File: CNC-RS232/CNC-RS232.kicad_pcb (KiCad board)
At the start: 2 copper layers, 100 x 80 mm, 50 parts, among them J1 DIN-5_180degree, J2 DIN-5_180degree, J3 DIN-5_180degree, J4 DIN-5_180degree, J5 DIN-5_180degree, Q1 BC547, Q2 BC557, Q3 BC547, Q4 BC547, U1 L7805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

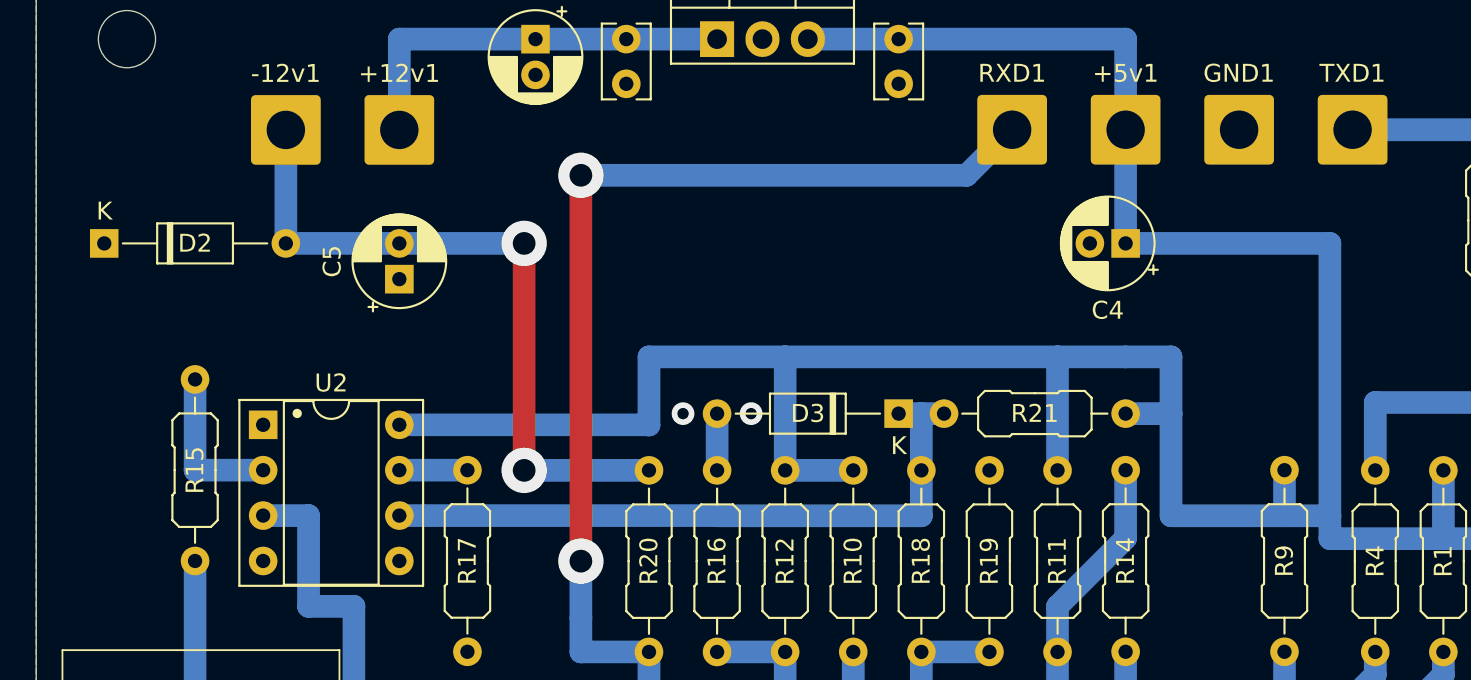
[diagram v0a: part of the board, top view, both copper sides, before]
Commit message: fixed RS232 and Thru
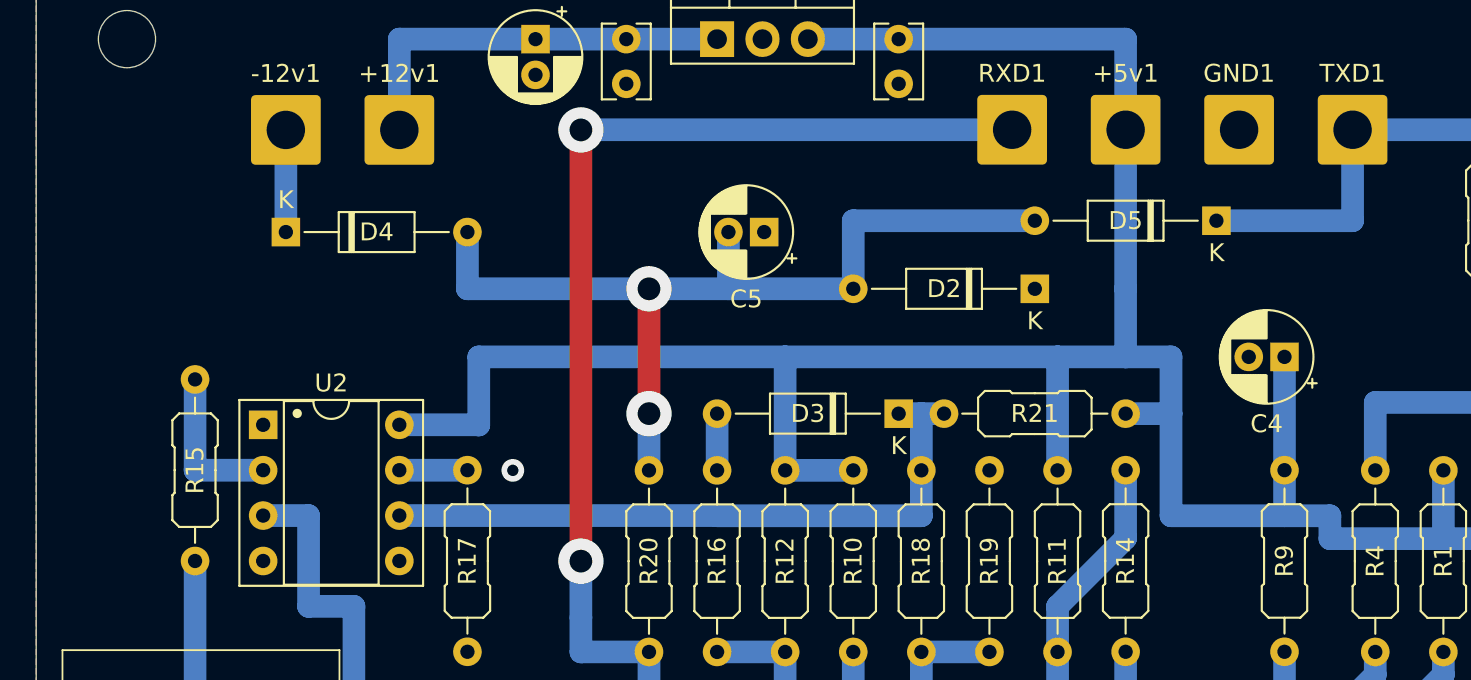
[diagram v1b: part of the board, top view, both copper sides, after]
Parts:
- added D4: 1N4148, Diode_THT:D_DO-35_SOD27_P10.16mm_Horizontal, F.Cu at (26.7, 28.6)
- added D5: 1N4148, Diode_THT:D_DO-35_SOD27_P10.16mm_Horizontal, F.Cu at (78.7, 27.9)
- moved D2 52.1 mm to (68.6, 31.8), turned to 180 degrees
- moved C5 20.6 mm to (53.4, 28.6), turned to 180 degrees
- moved C4 10.9 mm to (82.5, 35.6)
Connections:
- C5 pad 2: Net-(-12v1-Pin_1) -> Net-(D2-A)
- D2 pad 2: Net-(-12v1-Pin_1) -> Net-(D2-A)
- R20 pad 1: Net-(-12v1-Pin_1) -> Net-(D2-A)
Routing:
- net Net-(D2-A): track 0.00 -> 52.1 mm, vias 0 -> 2
- net Net-(-12v1-Pin_1): track 39.4 -> 5.71 mm, vias 2 -> 0
- net +5V: track 176.6 -> 162.6 mm
- net Net-(D5-K): track 7.62 -> 20.3 mm
- net Net-(Q2-C): track 63.6 -> 65.0 mm
- net GND: vias 2 -> 1

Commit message: PCB cleanup
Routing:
- net Net-(Q2-C): track 65.0 -> 64.3 mm
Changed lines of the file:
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@@
 	(segment
 		(start 43.18 46.99)
-		(end 43.18 22.86)
+		(end 43.18 24.13)
 		(width 1.27)
 		(layer "F.Cu")
@@
 	)
 	(via
-		(at 43.18 22.86)
+		(at 43.18 24.13)
 		(size 2.54)
 		(drill 1.27)
@@
 	)
 	(segment
-		(start 43.19 22.85)
-		(end 67.31 22.85)
+		(start 43.18 24.13)
+		(end 66.03 24.13)
 		(width 1.27)
 		(layer "B.Cu")
@@
 	)
 	(segment
-		(start 43.18 22.86)
-		(end 43.19 22.85)
+		(start 46.99 52.07)
+		(end 43.18 52.07)
 		(width 1.27)
 		(layer "B.Cu")
@@
 	)
 	(segment
-		(start 46.99 52.07)
-		(end 43.18 52.07)
+		(start 66.03 24.13)
+		(end 67.31 22.85)
 		(width 1.27)
 		(layer "B.Cu")
